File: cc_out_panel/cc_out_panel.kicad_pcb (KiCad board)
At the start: 2 copper layers, 103 x 53 mm, 2 parts

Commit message: update silk
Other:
- board text added: "ge020abe"
- board text removed: "g4574547"
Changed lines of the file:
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@@
     (effects (font (size 1 1) (thickness 0.15)) (justify right))
   )
-  (gr_text "g4574547" (at 142.0963 79.3567) (layer "F.SilkS")
+  (gr_text "ge020abe" (at 142.0963 79.3567) (layer "F.SilkS")
     (effects (font (size 1 1) (thickness 0.15)) (justify left))
   )

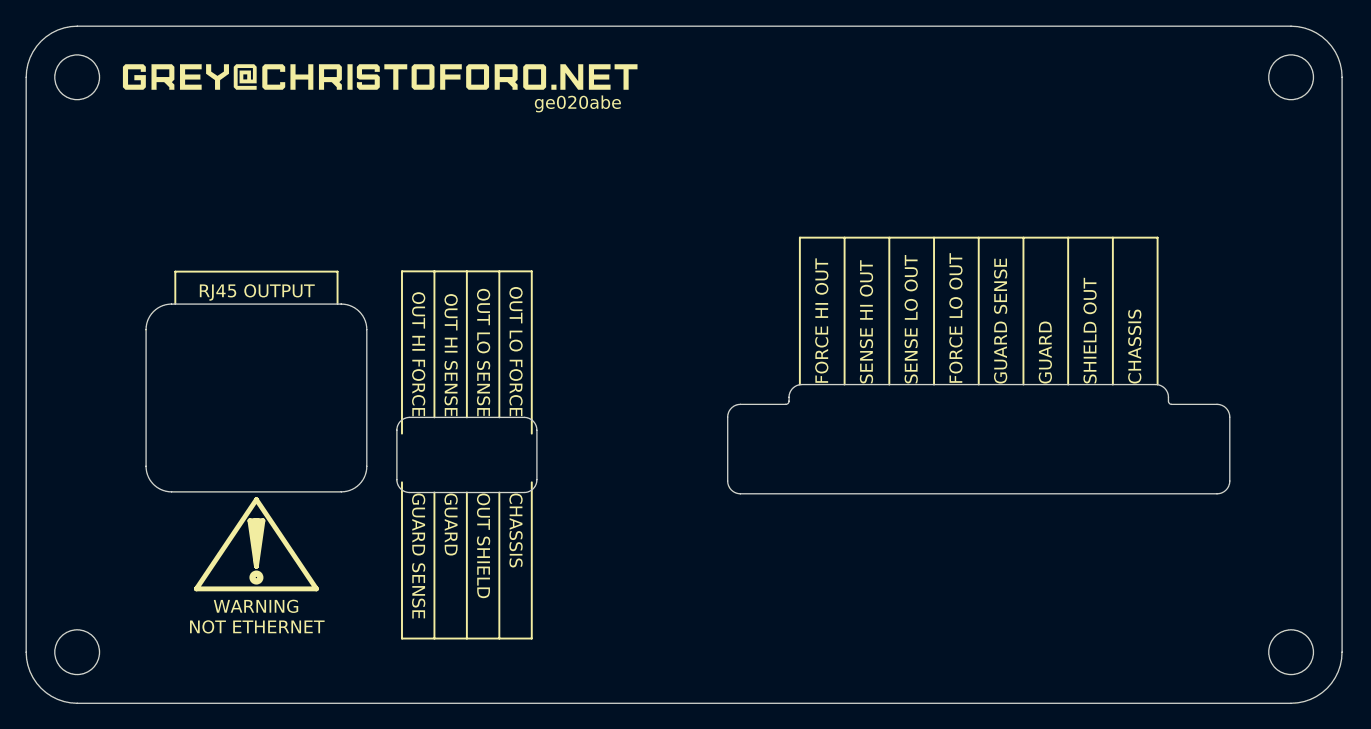
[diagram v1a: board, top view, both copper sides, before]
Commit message: new holder pcbs
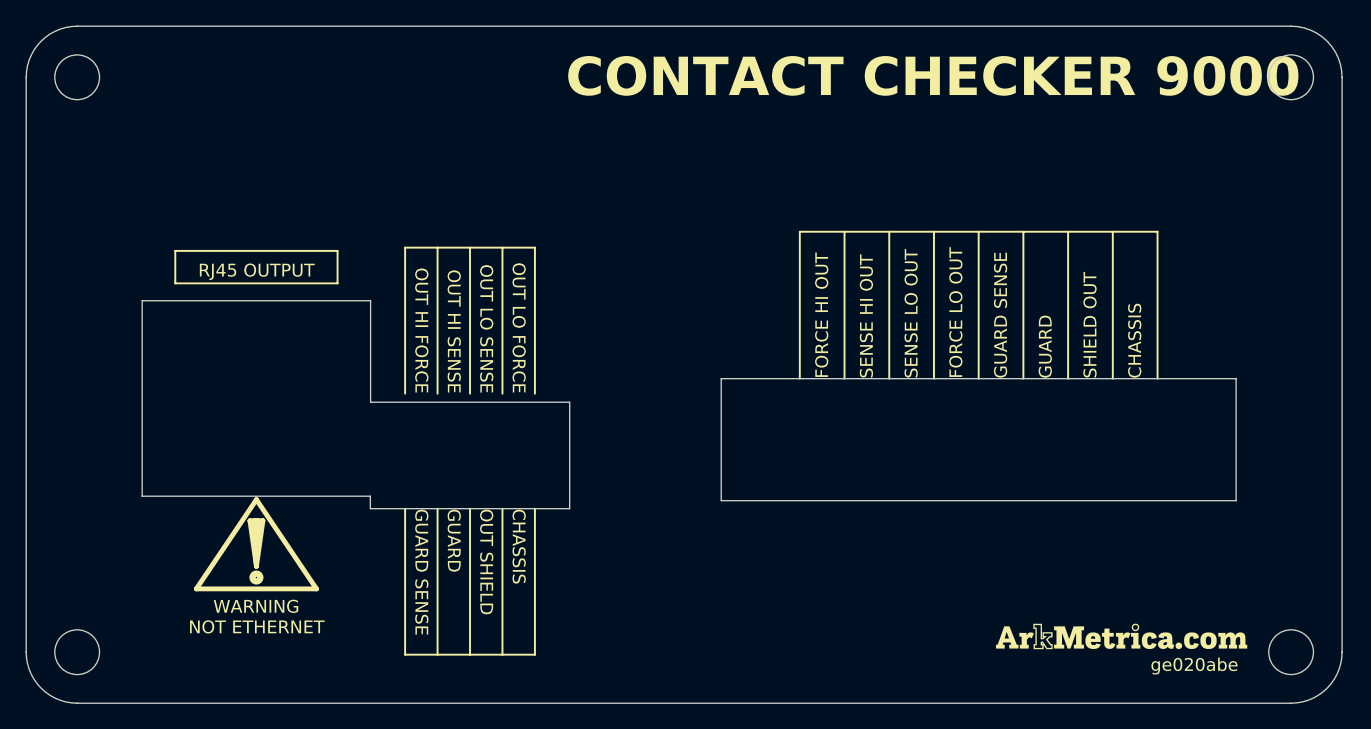
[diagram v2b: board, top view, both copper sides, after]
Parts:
- removed the G*** at (130.1, 77.4)
- added G***: LOGO, custom:site_small, F.Cu at (188.1, 121.1)
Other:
- outline, holes or cut-outs redrawn
- board text added: "CONTACT CHECKER 9000"

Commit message: update silk
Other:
- board text added: "b8007ef"
- board text removed: "ge020abe"
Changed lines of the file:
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@@
     (effects (font (size 1 1) (thickness 0.15)) (justify right))
   )
-  (gr_text "ge020abe" (at 190.3563 123.3567) (layer "F.SilkS")
+  (gr_text "b8007ef" (at 190.3563 123.3567) (layer "F.SilkS")
     (effects (font (size 1 1) (thickness 0.15)) (justify left))
   )

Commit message: plotted
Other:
- board text added: "cc9k"
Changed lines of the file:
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@@
     (grid_origin 137.096295 111.121704)
     (pcbplotparams
-      (layerselection 0x00010fc_ffffffff)
+      (layerselection 0x00010f0_ffffffff)
       (plot_on_all_layers_selection 0x0000000_00000000)
       (disableapertmacros false)
@@
       (outputformat 1)
       (mirror false)
-      (drillshape 1)
+      (drillshape 0)
       (scaleselection 1)
-      (outputdirectory "")
+      (outputdirectory "output")
     )
   )
@@
   (gr_line (start 197.061295 110.496404) (end 197.061295 100.946704)
     (stroke (width 0.1) (type solid)) (layer "Edge.Cuts"))
+  (gr_text "cc9k" (at 198.096295 117.121704) (layer "F.Cu")
+    (effects (font (size 1.5 1.5) (thickness 0.3) bold) (justify left bottom))
+  )
   (gr_text "GUARD" (at 182.161295 100.946704 90) (layer "F.SilkS")
     (effects (font (size 1 1) (thickness 0.15)) (justify left))

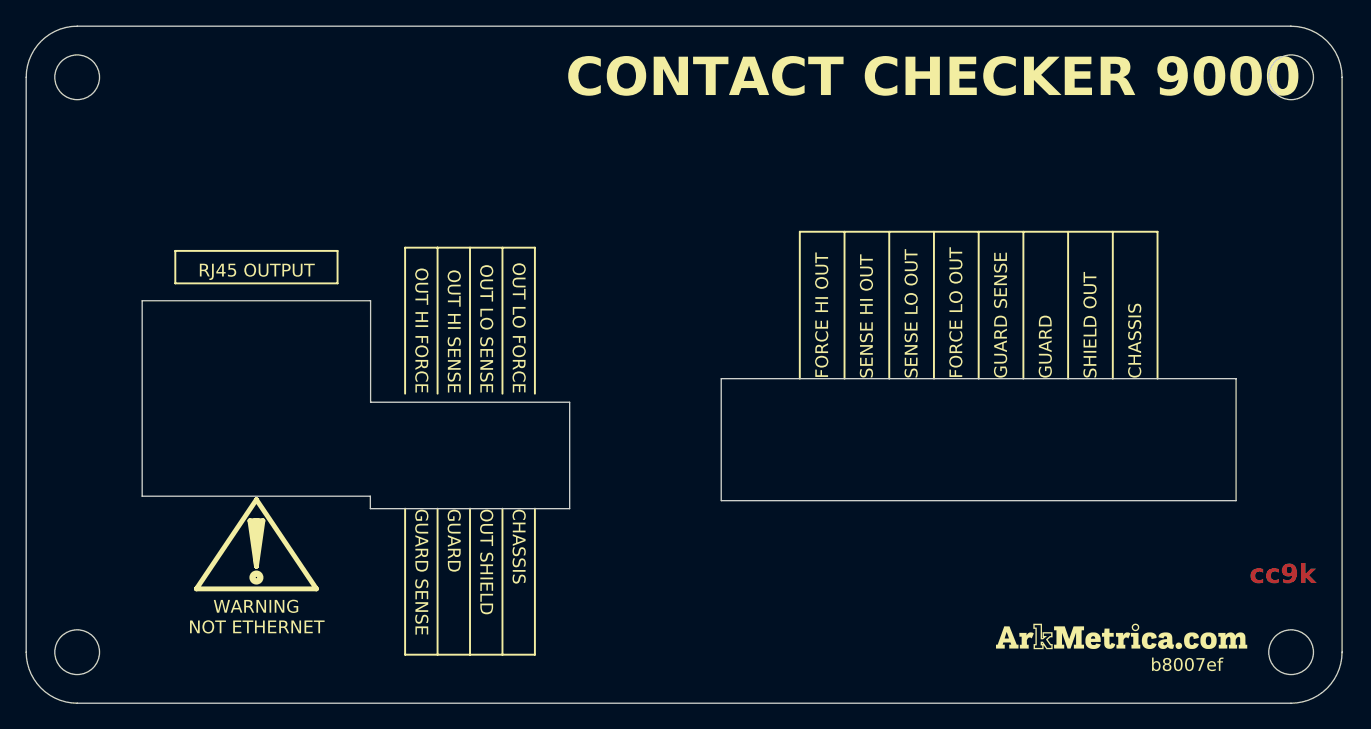
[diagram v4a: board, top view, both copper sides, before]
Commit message: upgrade contact checker with sense circuitry
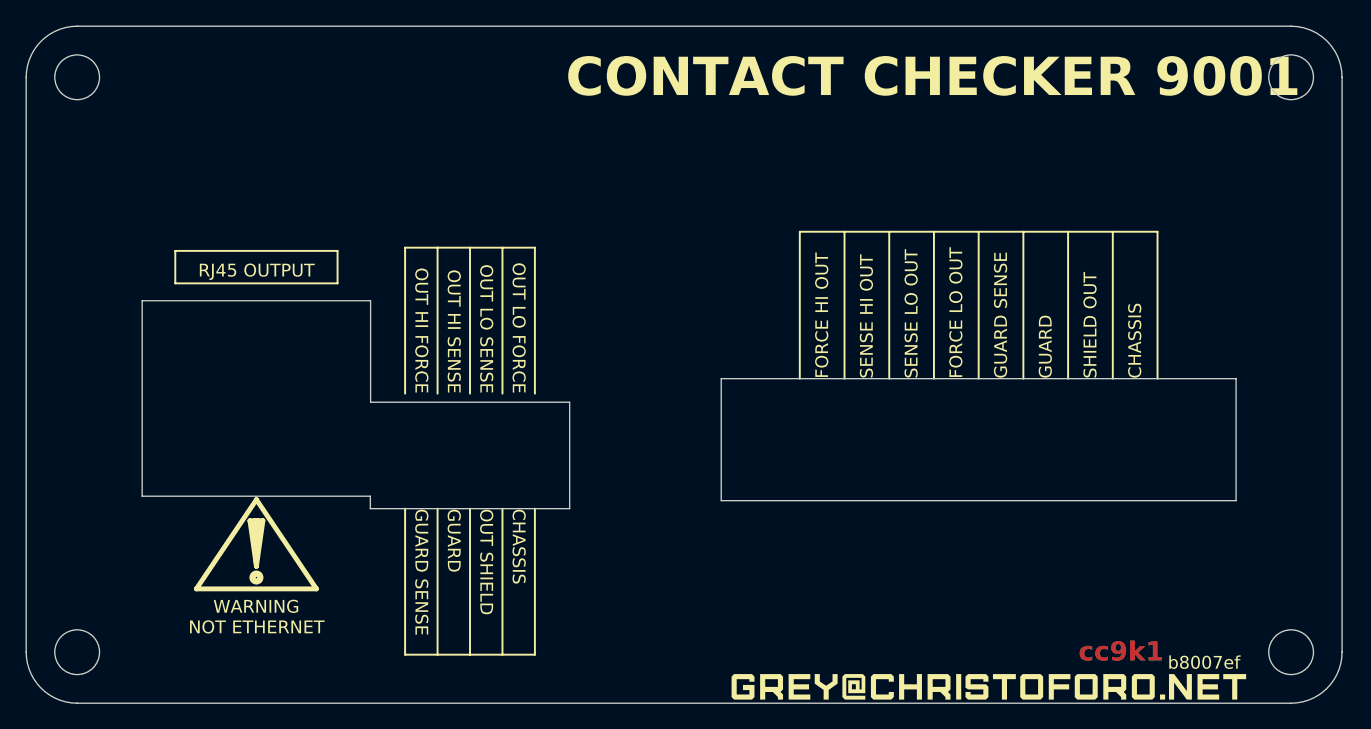
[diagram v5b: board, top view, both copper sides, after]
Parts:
- G***: footprint custom:site_small -> custom:logo
- moved G*** 11.1 mm to (177.7, 125.1)
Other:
- board text added: "CONTACT CHECKER 9001"
- board text added: "cc9k1"
- board text removed: "CONTACT CHECKER 9000"
- board text removed: "cc9k"

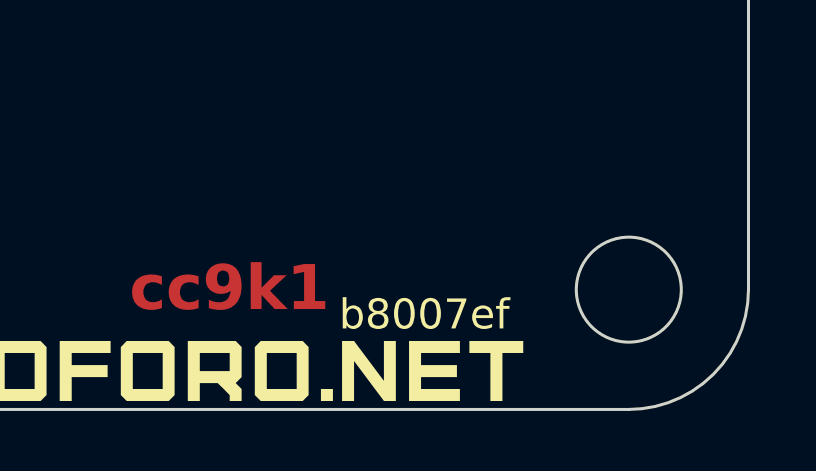
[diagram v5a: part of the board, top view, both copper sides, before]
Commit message: add some missing silkscreen
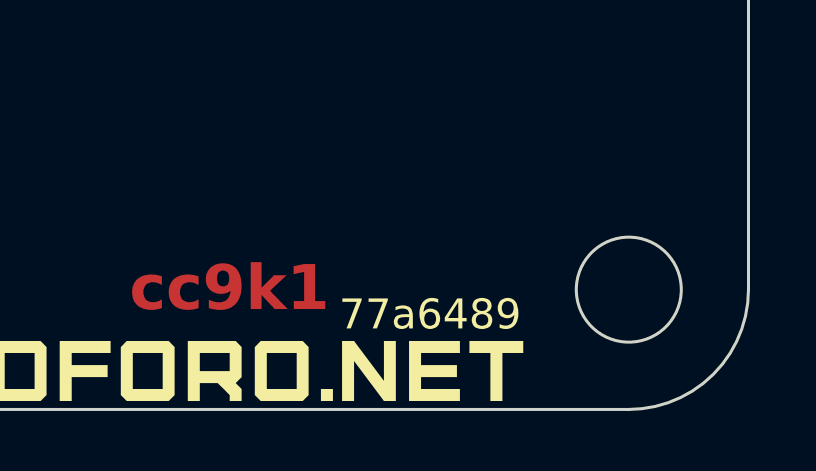
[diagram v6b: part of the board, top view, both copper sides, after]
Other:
- board text added: "77a6489"
- board text removed: "b8007ef"
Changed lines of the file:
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@@
     (effects (font (size 1 1) (thickness 0.15)) (justify right))
   )
-  (gr_text "b8007ef" (at 191.706295 123.186704) (layer "F.SilkS")
+  (gr_text "77a6489" (at 191.706295 123.186704) (layer "F.SilkS")
     (effects (font (size 1 1) (thickness 0.15)) (justify left))
   )

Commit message: update silk
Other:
- board text added: "c5b4c2a"
- board text removed: "77a6489"
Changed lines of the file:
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@@
     (effects (font (size 1 1) (thickness 0.15)) (justify right))
   )
-  (gr_text "77a6489" (at 191.706295 123.186704) (layer "F.SilkS")
+  (gr_text "c5b4c2a" (at 191.706295 123.186704) (layer "F.SilkS")
     (effects (font (size 1 1) (thickness 0.15)) (justify left))
   )

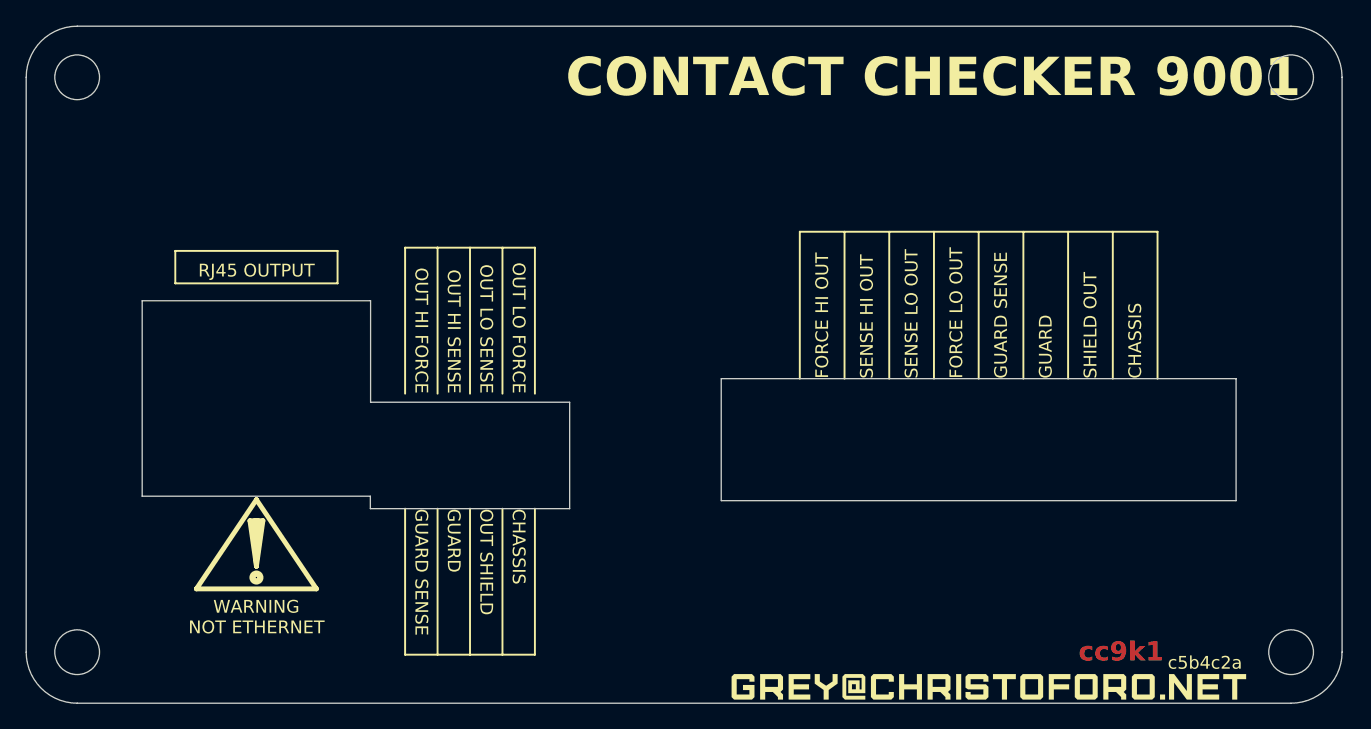
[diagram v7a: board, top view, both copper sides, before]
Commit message: fix up in&out cc panels
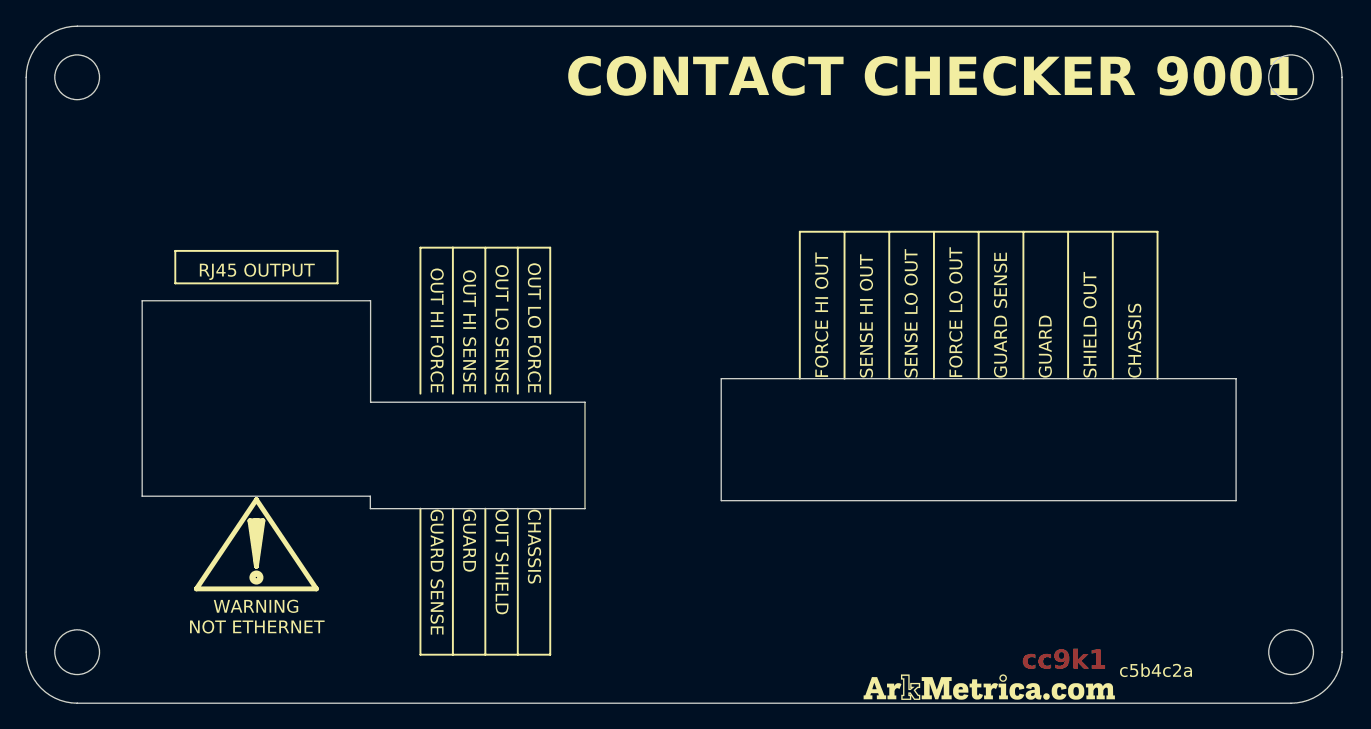
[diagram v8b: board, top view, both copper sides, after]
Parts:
- G***: footprint custom:logo -> custom:site_small
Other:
- outline, holes or cut-outs redrawn
